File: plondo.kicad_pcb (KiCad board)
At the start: 2 copper layers, 242.6 x 113.7 mm, 132 parts, among them J1 AVR ISP, J2 USB4085, SW0 MX_SW_HS, SW1 MX_SW_HS, SW10 MX_SW_HS, SW11 MX_SW_HS, SW12 MX_SW_HS, SW13 MX_SW_HS, SW14 MX_SW_HS, SW15 MX_SW_HS, SW16 MX_SW_HS, SW17 MX_SW_HS, SW18 MX_SW_HS, SW19 MX_SW_HS, SW2 MX_SW_HS, SW20 MX_SW_HS, SW21 MX_SW_HS, SW22 MX_SW_HS, SW23 MX_SW_HS, SW24 MX_SW_HS, SW25 MX_SW_HS, SW26 MX_SW_HS, SW27 MX_SW_HS, SW28 MX_SW_HS, SW29 MX_SW_HS, SW3 MX_SW_HS, SW30 MX_SW_HS, SW31 MX_SW_HS, SW32 MX_SW_HS, SW33 MX_SW_HS, SW34 MX_SW_HS, SW35 MX_SW_HS, SW36 MX_SW_HS, SW37 MX_SW_HS, SW38 MX_SW_HS, SW39 MX_SW_HS, SW4 MX_SW_HS, SW40 MX_SW_HS, SW41 MX_SW_HS, SW42 MX_SW_HS, SW43 MX_SW_HS, SW44 MX_SW_HS, SW45 MX_SW_HS, SW46 MX_SW_HS, SW47 MX_SW_HS, SW5 MX_SW_HS, SW6 MX_SW_HS, SW7 MX_SW_HS, SW8 MX_SW_HS, SW9 MX_SW_HS, U1 ATmega32A-P, Y1 16MHz

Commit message: a lot more connections
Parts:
- moved R4 7.62 mm to (228.6, 46.4), turned to 180 degrees
- moved R6 7.62 mm to (228.6, 52.7), turned to 180 degrees
- moved R5 7.61 mm to (228.6, 49.5), turned to 180 degrees
- moved R10 6.35 mm to (165.1, 49.5)
- moved R8 6.35 mm to (165.1, 55.9)
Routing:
- net GND: track 16.5 -> 297.0 mm, vias 0 -> 1
- net VCC: track 0.00 -> 222.3 mm, vias 0 -> 1
- net IND1: track 0.00 -> 146.2 mm
- net IND2: track 0.00 -> 139.3 mm
- net IND3: track 0.00 -> 132.4 mm
- net Net-(LED2-Pad1): track 0.00 -> 125.0 mm
- net SDA: track 0.00 -> 124.7 mm
- net Net-(LED3-Pad1): track 0.00 -> 117.2 mm
- net SCL: track 0.00 -> 116.9 mm
- net Net-(LED4-Pad1): track 0.00 -> 110.1 mm
- net ROW0: track 0.00 -> 82.8 mm
- net ROT_A: track 0.00 -> 66.1 mm
- net ROT_B: track 0.00 -> 63.6 mm
- net Net-(D49-Pad1): track 0.00 -> 33.8 mm
- net Net-(D48-Pad1): track 0.00 -> 30.7 mm
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
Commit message: connected all components on the pcb
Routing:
- net RESET: track 19.7 -> 79.5 mm, vias 0 -> 3
- net GND: track 297.0 -> 339.6 mm
- net VCC: track 222.3 -> 239.4 mm
- net SCK: track 0.00 -> 11.4 mm
- net MOSI: track 0.00 -> 8.83 mm
- net MISO: track 0.00 -> 6.30 mm
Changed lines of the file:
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@@
   (segment (start 241.808 34.544) (end 240.865 35.487) (width 0.25) (layer "F.Cu") (net 2))
   (segment (start 226.695 33.02) (end 223.52 33.02) (width 0.25) (layer "F.Cu") (net 2))
+  (segment (start 206.061443 34.563557) (end 200.66 39.965) (width 0.25) (layer "F.Cu") (net 2))
+  (segment (start 211.47 36.2) (end 209.833557 34.563557) (width 0.25) (layer "F.Cu") (net 2))
   (segment (start 246.126 34.544) (end 241.808 34.544) (width 0.25) (layer "F.Cu") (net 2))
-  (segment (start 223.647 59.055) (end 221.234 56.642) (width 0.25) (layer "F.Cu") (net 2))
+  (segment (start 241.935 59.055) (end 223.647 59.055) (width 0.25) (layer "F.Cu") (net 2))
   (segment (start 145.975 39.715) (end 163.905 39.715) (width 0.25) (layer "F.Cu") (net 2))
   (segment (start 196.215 34.965) (end 191.77 39.41) (width 0.25) (layer "F.Cu") (net 2))
   (segment (start 191.77 39.41) (end 191.77 43.18) (width 0.25) (layer "F.Cu") (net 2))
   (segment (start 240.865 35.67) (end 240.865 37.02) (width 0.25) (layer "F.Cu") (net 2))
-  (segment (start 241.935 59.055) (end 223.647 59.055) (width 0.25) (layer "F.Cu") (net 2))
   (segment (start 246.815 35.67) (end 246.815 37.02) (width 0.25) (layer "F.Cu") (net 2))
   (segment (start 239.690619 34.036) (end 227.711 34.036) (width 0.25) (layer "F.Cu") (net 2))
   (segment (start 254.37 53.34) (end 248.655 59.055) (width 0.25) (layer "F.Cu") (net 2))
   (segment (start 216.39637 61.595) (end 195.54 61.595) (width 0.25) (layer "F.Cu") (net 2))
-  (segment (start 245.745 59.055) (end 241.935 59.055) (width 0.25) (layer "F.Cu") (net 2))
+  (segment (start 223.647 59.055) (end 221.234 56.642) (width 0.25) (layer "F.Cu") (net 2))
   (segment (start 246.815 35.67) (end 246.815 35.233) (width 0.25) (layer "F.Cu") (net 2))
   (segment (start 240.865 35.487) (end 240.865 35.67) (width 0.25) (layer "F.Cu") (net 2))
@@
   (segment (start 200.66 39.41) (end 200.66 39.965) (width 0.25) (layer "F.Cu") (net 2))
   (segment (start 220.98 55.88) (end 220.98 57.01137) (width 0.25) (layer "F.Cu") (net 2))
+  (segment (start 245.745 59.055) (end 241.935 59.055) (width 0.25) (layer "F.Cu") (net 2))
   (segment (start 195.54 61.595) (end 195.54 59.65) (width 0.25) (layer "F.Cu") (net 2))
   (segment (start 239.014 43.942) (end 236.474 43.942) (width 0.25) (layer "F.Cu") (net 2))
@@
   (segment (start 227.711 34.036) (end 226.695 33.02) (width 0.25) (layer "F.Cu") (net 2))
   (segment (start 220.98 57.01137) (end 216.39637 61.595) (width 0.25) (layer "F.Cu") (net 2))
+  (segment (start 209.833557 34.563557) (end 206.061443 34.563557) (width 0.25) (layer "F.Cu") (net 2))
   (via (at 239.014 43.942) (size 0.8) (drill 0.4) (layers "F.Cu" "B.Cu") (net 2))
+  (segment (start 238.506 49.276) (end 238.506 53.34) (width 0.25) (layer "B.Cu") (net 2))
   (segment (start 145.975 39.715) (end 145.975 43.821) (width 0.25) (layer "B.Cu") (net 2))
   (segment (start 198.033 34.965) (end 200.66 37.592) (width 0.25) (layer "B.Cu") (net 2))
   (segment (start 240.865 37.02) (end 240.865 42.091) (width 0.25) (layer "B.Cu") (net 2))
   (segment (start 234.95 47.395) (end 234.95 41.275) (width 0.25) (layer "B.Cu") (net 2))
+  (segment (start 220.34 36.2) (end 223.52 33.02) (width 0.25) (layer "B.Cu") (net 2))
   (segment (start 163.905 39.715) (end 174.955 39.715) (width 0.25) (layer "B.Cu") (net 2))
   (segment (start 145.975 43.821) (end 144.018 45.778) (width 0.25) (layer "B.Cu") (net 2))
@@
   (segment (start 200.66 37.592) (end 200.66 39.965) (width 0.25) (layer "B.Cu") (net 2))
   (segment (start 234.95 41.275) (end 226.695 33.02) (width 0.25) (layer "B.Cu") (net 2))
+  (segment (start 241.935 56.769) (end 241.935 59.055) (width 0.25) (layer "B.Cu") (net 2))
   (segment (start 240.865 42.091) (end 239.014 43.942) (width 0.25) (layer "B.Cu") (net 2))
   (segment (start 74.353 45.778) (end 71.755 43.18) (width 0.25) (layer "B.Cu") (net 2))
+  (segment (start 238.506 53.34) (end 241.935 56.769) (width 0.25) (layer "B.Cu") (net 2))
   (segment (start 144.018 45.778) (end 74.353 45.778) (width 0.25) (layer "B.Cu") (net 2))
   (segment (start 196.215 34.965) (end 179.705 34.965) (width 0.25) (layer "B.Cu") (net 2))
+  (segment (start 234.95 47.395) (end 236.625 47.395) (width 0.25) (layer "B.Cu") (net 2))
   (segment (start 174.955 39.715) (end 179.705 34.965) (width 0.25) (layer "B.Cu") (net 2))
+  (segment (start 211.47 36.2) (end 220.34 36.2) (width 0.25) (layer "B.Cu") (net 2))
+  (segment (start 236.625 47.395) (end 238.506 49.276) (width 0.25) (layer "B.Cu") (net 2))
   (segment (start 163.905 48.335) (end 163.905 39.715) (width 0.25) (layer "B.Cu") (net 2))
   (segment (start 61.468 44.196) (end 68.199 44.196) (width 0.25) (layer "F.Cu") (net 3))
@@
   (segment (start 144.321402 44.45) (end 161.544 44.45) (width 0.25) (layer "F.Cu") (net 3))
   (segment (start 230.886 54.356) (end 231.775 55.245) (width 0.25) (layer "F.Cu") (net 3))
+  (segment (start 197.485 52.705) (end 194.31 49.53) (width 0.25) (layer "F.Cu") (net 3))
   (segment (start 59.69 42.418) (end 61.468 44.196) (width 0.25) (layer "F.Cu") (net 3))
   (segment (start 220.98 52.705) (end 197.485 52.705) (width 0.25) (layer "F.Cu") (net 3))
@@
   (segment (start 231.775 55.245) (end 233.68 55.245) (width 0.25) (layer "F.Cu") (net 3))
   (segment (start 190.54 61.595) (end 190.54 59.65) (width 0.25) (layer "F.Cu") (net 3))
+  (segment (start 194.31 49.53) (end 194.31 43.18) (width 0.25) (layer "F.Cu") (net 3))
   (segment (start 234.95 48.895) (end 238.115 48.895) (width 0.25) (layer "F.Cu") (net 3))
   (segment (start 238.115 48.895) (end 241.3 45.71) (width 0.25) (layer "F.Cu") (net 3))
@@
   (segment (start 179.705 46.355) (end 191.77 58.42) (width 0.25) (layer "F.Cu") (net 3))
   (via (at 143.774753 44.996649) (size 0.8) (drill 0.4) (layers "F.Cu" "B.Cu") (net 3))
+  (segment (start 201.895 36.2) (end 200.66 34.965) (width 0.25) (layer "B.Cu") (net 3))
   (segment (start 121.412 45.328) (end 143.443402 45.328) (width 0.25) (layer "B.Cu") (net 3))
+  (segment (start 206.39 36.2) (end 201.895 36.2) (width 0.25) (layer "B.Cu") (net 3))
   (segment (start 143.443402 45.328) (end 143.774753 44.996649) (width 0.25) (layer "B.Cu") (net 3))
   (segment (start 76.443 45.328) (end 121.412 45.328) (width 0.25) (layer "B.Cu") (net 3))
@@
   (segment (start 257.81 123.952) (end 262.122 123.952) (width 0.25) (layer "B.Cu") (net 55))
   (segment (start 262.122 123.952) (end 267.71 129.54) (width 0.25) (layer "B.Cu") (net 55))
+  (segment (start 206.37 38.74) (end 201.93 43.18) (width 0.25) (layer "B.Cu") (net 56))
+  (segment (start 206.39 38.74) (end 206.37 38.74) (width 0.25) (layer "B.Cu") (net 56))
+  (segment (start 205.943601 41.726399) (end 200.843601 41.726399) (width 0.25) (layer "F.Cu") (net 57))
+  (segment (start 208.93 38.74) (end 205.943601 41.726399) (width 0.25) (layer "F.Cu") (net 57))
+  (segment (start 200.843601 41.726399) (end 199.39 43.18) (width 0.25) (layer "F.Cu") (net 57))
+  (segment (start 207.755 39.895) (end 204.47 43.18) (width 0.25) (layer "B.Cu") (net 58))
+  (segment (start 208.93 36.2) (end 207.755 37.375) (width 0.25) (layer "B.Cu") (net 58))
+  (segment (start 207.755 37.375) (end 207.755 39.895) (width 0.25) (layer "B.Cu") (net 58))
+  (segment (start 210.295 37.565) (end 205.259 37.565) (width 0.25) (layer "F.Cu") (net 59))
+  (segment (start 201.547601 41.276399) (end 198.753601 41.276399) (width 0.25) (layer "F.Cu") (net 59))
+  (segment (start 196.85 44.704) (end 196.85 43.18) (width 0.25) (layer "F.Cu") (net 59))
+  (segment (start 162.814 42.164) (end 164.846 42.164) (width 0.25) (layer "F.Cu") (net 59))
+  (segment (start 211.47 38.74) (end 210.295 37.565) (width 0.25) (layer "F.Cu") (net 59))
+  (segment (start 196.364704 45.189296) (end 196.85 44.704) (width 0.25) (layer "F.Cu") (net 59))
   (segment (start 145.975 35.215) (end 152.475 35.215) (width 0.25) (layer "F.Cu") (net 59))
+  (segment (start 195.58 45.189296) (end 196.364704 45.189296) (width 0.25) (layer "F.Cu") (net 59))
+  (segment (start 205.259 37.565) (end 201.547601 41.276399) (width 0.25) (layer "F.Cu") (net 59))
+  (segment (start 198.753601 41.276399) (end 196.85 43.18) (width 0.25) (layer "F.Cu") (net 59))
+  (via (at 195.58 45.189296) (size 0.8) (drill 0.4) (layers "F.Cu" "B.Cu") (net 59))
+  (via (at 164.846 42.164) (size 0.8) (drill 0.4) (layers "F.Cu" "B.Cu") (net 59))
+  (via (at 162.814 42.164) (size 0.8) (drill 0.4) (layers "F.Cu" "B.Cu") (net 59))
   (segment (start 152.475 37.159) (end 157.48 42.164) (width 0.25) (layer "B.Cu") (net 59))
   (segment (start 152.475 35.215) (end 152.475 37.159) (width 0.25) (layer "B.Cu") (net 59))
   (segment (start 157.48 42.164) (end 157.48 46.355) (width 0.25) (layer "B.Cu") (net 59))
+  (segment (start 168.633296 45.189296) (end 195.58 45.189296) (width 0.25) (layer "B.Cu") (net 59))
+  (segment (start 157.48 42.164) (end 162.814 42.164) (width 0.25) (layer "B.Cu") (net 59))
+  (segment (start 165.608 42.164) (end 168.633296 45.189296) (width 0.25) (layer "B.Cu") (net 59))
+  (segment (start 164.846 42.164) (end 165.608 42.164) (width 0.25) (layer "B.Cu") (net 59))
   (segment (start 245.115 38.095) (end 244.348 38.862) (width 0.25) (layer "B.Cu") (net 60))
   (segment (start 244.348 38.862) (end 244.348 50.038) (width 0.25) (layer "B.Cu") (net 60))

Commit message: rounded corners!
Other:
- board size 242.6 x 113.7 mm -> 243.8 x 114.3 mm
- board text added: "114.30mm"
- board text added: "243.84mm"
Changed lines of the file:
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@@
     )
   )
-  (gr_rect (start 28.575 144.145) (end 271.145 30.48) (layer "Edge.Cuts") (width 0.1) (fill none))
+  (gr_line (start 27.94 151.13) (end 27.94 156.21) (layer "Eco1.User") (width 0.5))
+  (gr_line (start 27.94 153.67) (end 271.78 153.67) (layer "Eco1.User") (width 0.5))
+  (gr_line (start 276.86 30.48) (end 281.94 30.48) (layer "Eco1.User") (width 0.5))
+  (gr_line (start 279.4 30.48) (end 279.4 144.78) (layer "Eco1.User") (width 0.5))
+  (gr_line (start 276.86 144.78) (end 281.94 144.78) (layer "Eco1.User") (width 0.5))
+  (gr_line (start 271.78 151.13) (end 271.78 156.21) (layer "Eco1.User") (width 0.5))
+  (gr_arc (start 271.78 142.24) (mid 271.036051 144.036051) (end 269.24 144.78) (layer "Edge.Cuts") (width 0.1))
+  (gr_line (start 269.24 144.78) (end 30.48 144.78) (layer "Edge.Cuts") (width 0.1))
+  (gr_line (start 30.48 30.48) (end 269.24 30.48) (layer "Edge.Cuts") (width 0.1))
+  (gr_arc (start 27.94 33.02) (mid 28.683949 31.223949) (end 30.48 30.48) (layer "Edge.Cuts") (width 0.1))
+  (gr_arc (start 30.48 144.78) (mid 28.683949 144.036051) (end 27.94 142.24) (layer "Edge.Cuts") (width 0.1))
+  (gr_arc (start 269.24 30.48) (mid 271.036051 31.223949) (end 271.78 33.02) (layer "Edge.Cuts") (width 0.1))
+  (gr_line (start 27.94 142.24) (end 27.94 33.02) (layer "Edge.Cuts") (width 0.1))
+  (gr_line (start 271.78 33.02) (end 271.78 142.24) (layer "Edge.Cuts") (width 0.1))
+  (gr_text "243.84mm\n" (at 156.21 158.75) (layer "Eco1.User")
+    (effects (font (size 3 3) (thickness 0.5)))
+  )
+  (gr_text "114.30mm" (at 294.64 88.9) (layer "Eco1.User")
+    (effects (font (size 3 3) (thickness 0.5)))
+  )
   (segment (start 157.405 35.215) (end 163.905 35.215) (width 0.25) (layer "F.Cu") (net 1))
   (segment (start 176.53 43.18) (end 176.53 36.576) (width 0.25) (layer "F.Cu") (net 1))

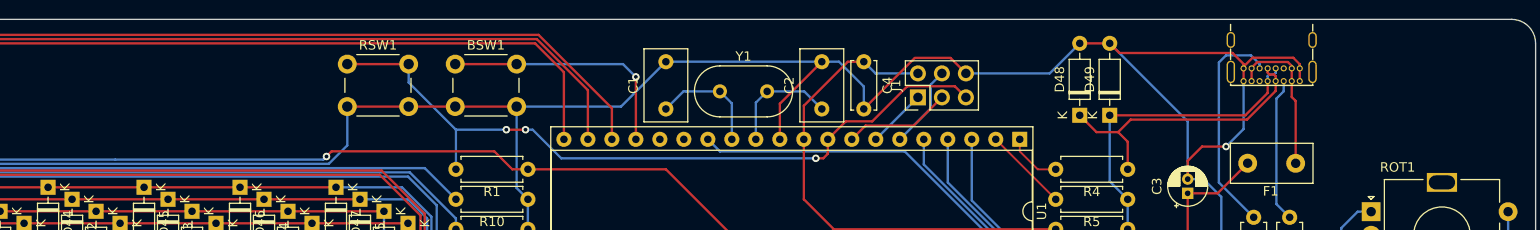
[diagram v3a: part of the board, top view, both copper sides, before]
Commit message: add nice silkscreen stuff, update readme
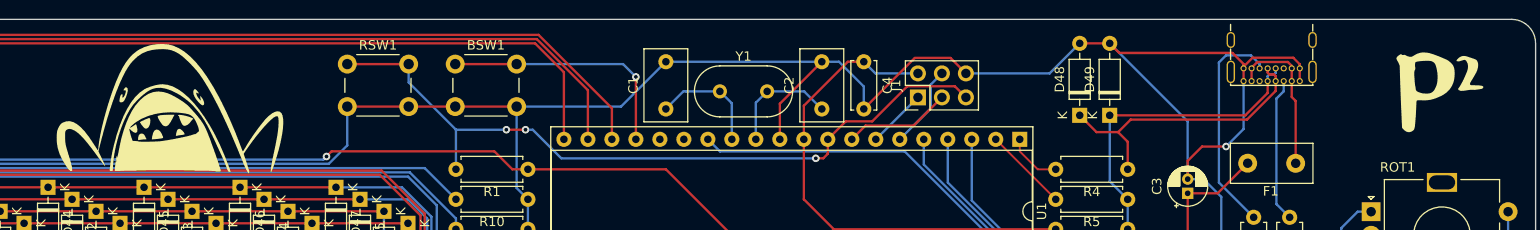
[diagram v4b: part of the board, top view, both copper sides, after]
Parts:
- added G***: LOGO, plondo:blahaj, F.Cu at (127.0, 40.6)
- added G***: LOGO, plondo:plondo, F.Cu at (261.6, 38.1)
